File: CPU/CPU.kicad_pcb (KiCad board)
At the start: 2 copper layers, 157.1 x 85.3 mm, 100 parts, among them J101 Conn_02x10_Odd_Even, J102 Conn_02x14_Odd_Even_MountingP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, J301 Conn_02x03_Odd_Even, J302 1X4SMD-FPC, J303 Conn_02x03_Odd_Even, Q101 IRLML0040TR, Q102 IRLML0040TR, Q201 DMC4050, Q301 IRLML0040TR, Q302 IRLML0040TR, SW101 SW_SPDT, SW301 TACTILE_SWITCHPTS540-SMD, SW302 TACTILE_SWITCHPTS540-SMD, SW303 TACTILE_SWITCHPTS540-SMD, SW304 TACTILE_SWITCHPTS540-SMD, SW305 TACTILE_SWITCHPTS540-SMD, SW306 TACTILE_SWITCHPTS540-SMD, SW307 TACTILE_SWITCHPTS540-SMD, SW308 TACTILE_SWITCHPTS540-SMD, SW309 TACTILE_SWITCHPTS540-SMD, SW310 TACTILE_SWITCHPTS540-SMD, SW311 TACTILE_SWITCHPTS540-SMD, SW312 TACTILE_SWITCHPTS540-SMD, SW313 TACTILE_SWITCHPTS540-SMD, U201 OPT3001, U202 ATtiny1614-SS, U301 ATmega328PB-AU, Y301 Resonator_Small

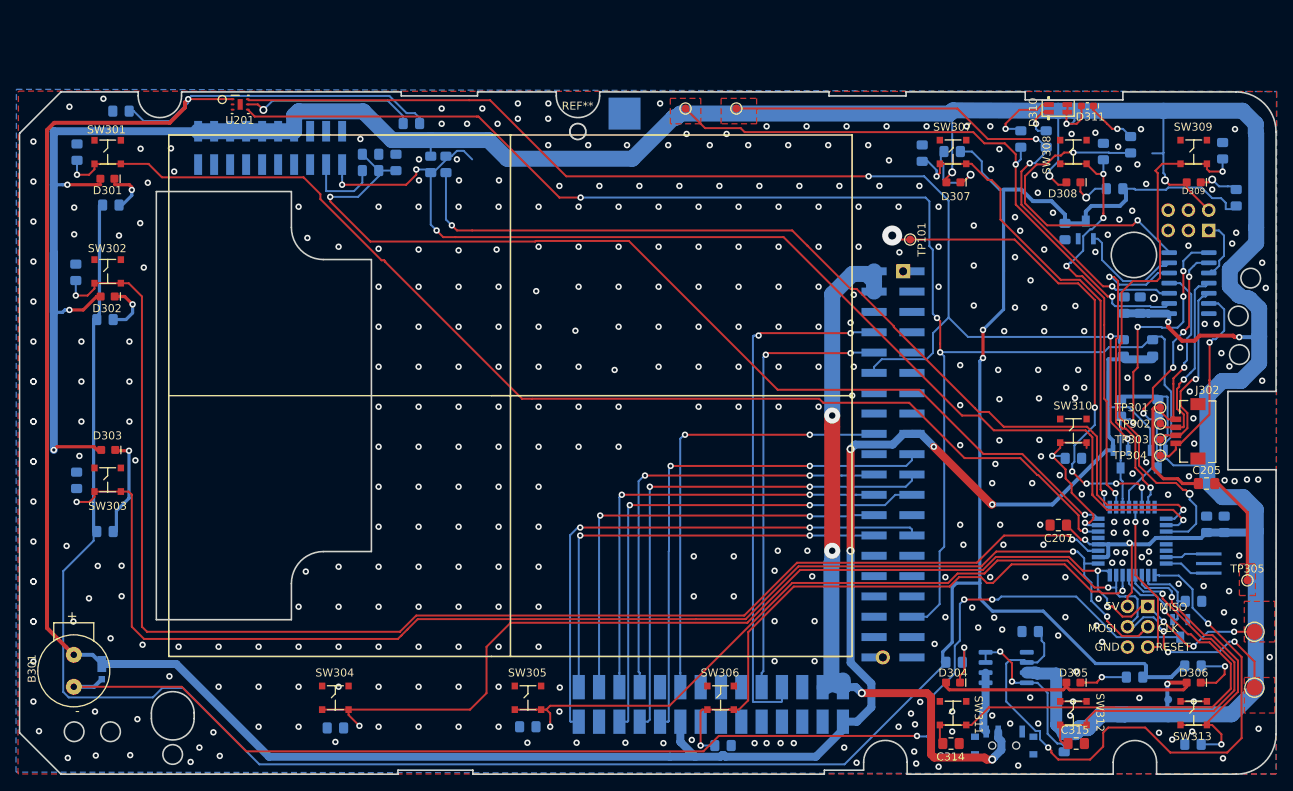
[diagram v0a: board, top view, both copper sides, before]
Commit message: Renaming components.
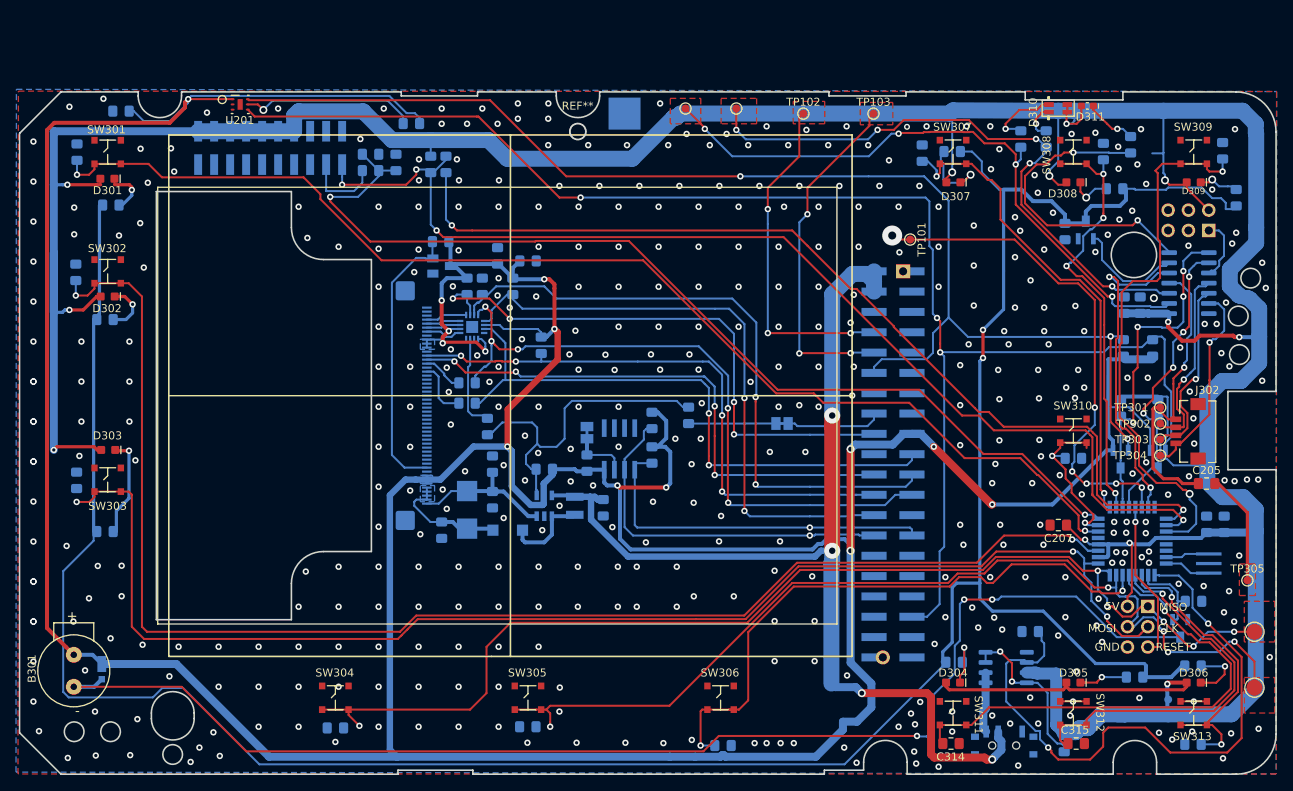
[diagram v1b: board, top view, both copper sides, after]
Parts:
- removed J102: Conn_02x14_Odd_Even_MountingPin, CPU:2X14_SMT_MALE-2
- added C1: 10uF, Capacitor_SMD:C_0805_2012Metric_Pad1.15x1.40mm_HandSolder, B.Cu at (94.0, 66.7)
- added C16: 10uF, Capacitor_SMD:C_0805_2012Metric_Pad1.15x1.40mm_HandSolder, B.Cu at (103.4, 97.5)
- added C18: 0.1uF, Capacitor_SMD:C_0805_2012Metric_Pad1.15x1.40mm_HandSolder, B.Cu at (89.5, 96.5)
- added C20: 1uF, Capacitor_SMD:C_0805_2012Metric_Pad1.15x1.40mm_HandSolder, B.Cu at (83.2, 100.3)
- added C4: 0.1uF, Capacitor_SMD:C_0805_2012Metric_Pad1.15x1.40mm_HandSolder, B.Cu at (90.2, 66.0)
- added D1: MM3Z24VT1G, PiTFT:SMADIODE, B.Cu at (86.4, 97.8)
- added D2: MBR0540, PiTFT:SOD-123, B.Cu at (91.4, 100.3)
- added IC5: AXP803, PiTFT:SOT23, B.Cu at (83.2, 67.3)
- added L1: 10uH 1007, PiTFT:INDUCTOR_1007, B.Cu at (99.8, 97.3)
- added R1: 12Ω, Resistor_SMD:R_0805_2012Metric_Pad1.15x1.40mm_HandSolder, B.Cu at (89.5, 92.1)
- added R10: 1K, Resistor_SMD:R_0805_2012Metric_Pad1.15x1.40mm_HandSolder, B.Cu at (114.0, 86.0)
- added R11: 10K, Resistor_SMD:R_0805_2012Metric_Pad1.15x1.40mm_HandSolder, B.Cu at (88.3, 69.8)
- added R12: 3.9K, Resistor_SMD:R_0805_2012Metric_Pad1.15x1.40mm_HandSolder, B.Cu at (109.5, 90.9)
- added R13: 3.9K, Resistor_SMD:R_0805_2012Metric_Pad1.15x1.40mm_HandSolder, B.Cu at (109.5, 86.6)
- added R14: 3.9K, Resistor_SMD:R_0805_2012Metric_Pad1.15x1.40mm_HandSolder, B.Cu at (101.3, 91.9)
- added R2: 10K, Resistor_SMD:R_0805_2012Metric_Pad1.15x1.40mm_HandSolder, B.Cu at (96.0, 92.7)
- added R3: 12, Resistor_SMD:R_0805_2012Metric_Pad1.15x1.40mm_HandSolder, B.Cu at (86.4, 84.5)
- added R4: 12, Resistor_SMD:R_0805_2012Metric_Pad1.15x1.40mm_HandSolder, B.Cu at (86.4, 81.9)
- added R5: 10K, Resistor_SMD:R_0805_2012Metric_Pad1.15x1.40mm_HandSolder, B.Cu at (95.6, 77.2)
- added R6: 10K, Resistor_SMD:R_0805_2012Metric_Pad1.15x1.40mm_HandSolder, B.Cu at (83.1, 64.3)
- added R7: 10K, Resistor_SMD:R_0805_2012Metric_Pad1.15x1.40mm_HandSolder, B.Cu at (92.1, 69.8)
- added R8: DNP, Resistor_SMD:R_0805_2012Metric_Pad1.15x1.40mm_HandSolder, B.Cu at (86.4, 69.8)
- added R9: 1K, Resistor_SMD:R_0805_2012Metric_Pad1.15x1.40mm_HandSolder, B.Cu at (88.9, 87.4)
- added SJ1: WP, PiTFT:SOLDERJUMPER_CLOSEDWIRE, B.Cu at (101.3, 88.1)
- added SJ2: SOLDERJUMPERCLOSED, PiTFT:SOLDERJUMPER_CLOSEDWIRE, B.Cu at (125.7, 87.0)
- added TP102: PiTX, TestPoint:TestPoint_Pad_D1.0mm, F.Cu at (128.4, 48.3)
- added TP103: PiRX, TestPoint:TestPoint_Pad_D1.0mm, F.Cu at (137.2, 48.3)
- added U1: CAT24C32, PiTFT:SOIC8_150MIL, B.Cu at (105.4, 90.2)
- added U2: STMPE610, PiTFT:QFN16_3MM, B.Cu at (87.0, 74.9)
- added U3: FAN5333BSX, PiTFT:SOT23-5@1, B.Cu at (96.0, 97.3)
- added X1: DISP_LCD_3.5IN_320X480_50PIN, PiTFT:TFT_3.5IN_320X480_50PIN, F.Cu at (85.1, 84.8)
- TP201: value TestPoint -> GND
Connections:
- Pi101 pad 10: /UARTB -> /PiRX
- Pi101 pad 16: Net-(Pi101-Pad16) -> /LCD_BACK_LIGHT
- Pi101 pad 8: /UARTA -> /PiTX
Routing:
- net +3V3: track 346.7 -> 556.3 mm, vias 5 -> 14
- net /UARTA: track 66.4 -> 0.00 mm, vias 2 -> 0
- net /UARTB: track 55.4 -> 0.00 mm, vias 2 -> 0
- net /PiRX: track 0.00 -> 43.2 mm, vias 0 -> 3
- net /PiTX: track 0.00 -> 42.6 mm, vias 0 -> 3
- net /Display/LCD_LITE: track 0.00 -> 40.9 mm
- net /Pi5V: track 92.0 -> 132.2 mm
- net /Display/TFT_RST: track 0.00 -> 35.2 mm
- net /EEDATA: track 68.3 -> 45.5 mm, vias 2 -> 1
- net /RT_CS: track 55.8 -> 76.3 mm
- net /SCLK: track 64.0 -> 83.6 mm, vias 2 -> 5
- net /Display/LEDK: track 0.00 -> 18.1 mm
- net /TFT_CS: track 55.7 -> 72.7 mm, vias 2 -> 4
- net /MISO: track 64.3 -> 80.7 mm
- net /RT_INIT: track 55.5 -> 71.8 mm, vias 2 -> 4
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- added copper zone on B.Cu, net +24V
- added copper zone on B.Cu, net +3V3
- added copper zone on F.Cu, net /PiRX
- added copper zone on F.Cu, net /PiTX
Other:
- board text added: "CR101 CPU Board V3 mquezada 20200519"
- board text removed: "CR101 CPU Board V2 mquezada 20200423"

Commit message: Add display circuitry.
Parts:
- D201: value Schottky -> Zener
- IC5: value AXP803 -> MAX803
- R3, R4: value 12 -> 12Ω
- U2: value STMPE610 -> STMPE811
- moved TP201 0.51 mm to (106.0, 48.8)
- moved C16 0.25 mm to (103.6, 97.5)
- turned R1 to 90 degrees
- turned R10 to 90 degrees
- turned R2 to 180 degrees
- turned R5 to 270 degrees
- turned R9 to 270 degrees
- renumbered C304 to C201, C305 to C202, C306 to C203, C307 to C204, C308 to C205, C309 to C206, C310 to C207, C311 to C208, C312 to C209, C313 to C210, C314 to C211, C315 to C212, C316 to C213, C206 to C214, C207 to C215, C301 to C216, C303 to C217, C201 to C301, C203 to C302, C202 to C303, C204 to C304, C205 to C305, J301 to J201, Q302 to Q202, R201 to R313, SW301 to SW201, SW302 to SW202, SW303 to SW203, SW304 to SW204, SW305 to SW205, SW306 to SW206, SW307 to SW207, SW308 to SW208, SW309 to SW209, SW310 to SW210, SW311 to SW211, SW312 to SW212, SW313 to SW213, U301 to U201, U201 to U301, U202 to U302, Y301 to Y201
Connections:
- R1 pad 1: GND -> /Display/LEDK
- R1 pad 2: /Display/LEDK -> GND
- R10 pad 1: /Display/LCD_LITE -> Net-(R10-Pad1)
- R10 pad 2: Net-(R10-Pad2) -> /Display/LCD_LITE
- R2 pad 1: /Display/LCD_LITE -> +3V3
- R2 pad 2: +3V3 -> /Display/LCD_LITE
- R5 pad 1: /TFT_CS -> +3V3
- R5 pad 2: +3V3 -> /TFT_CS
- R9 pad 1: /Display/LCD_LITE -> Net-(R9-Pad1)
- R9 pad 2: Net-(R9-Pad2) -> /Display/LCD_LITE
- SJ2 pad 2: Net-(R10-Pad2) -> Net-(R10-Pad1)
- U2 pad 11: Net-(R9-Pad2) -> Net-(R9-Pad1)
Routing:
- net Net-(R9-Pad2): track 11.8 -> 0.00 mm
- net Net-(R9-Pad1): track 0.00 -> 11.8 mm
- net Net-(R10-Pad2): track 10.9 -> 0.00 mm
- net Net-(R10-Pad1): track 0.00 -> 10.9 mm
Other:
- board text added: "LCD interface circuit by Adafruit. Referenced from PiTFT 3.5""

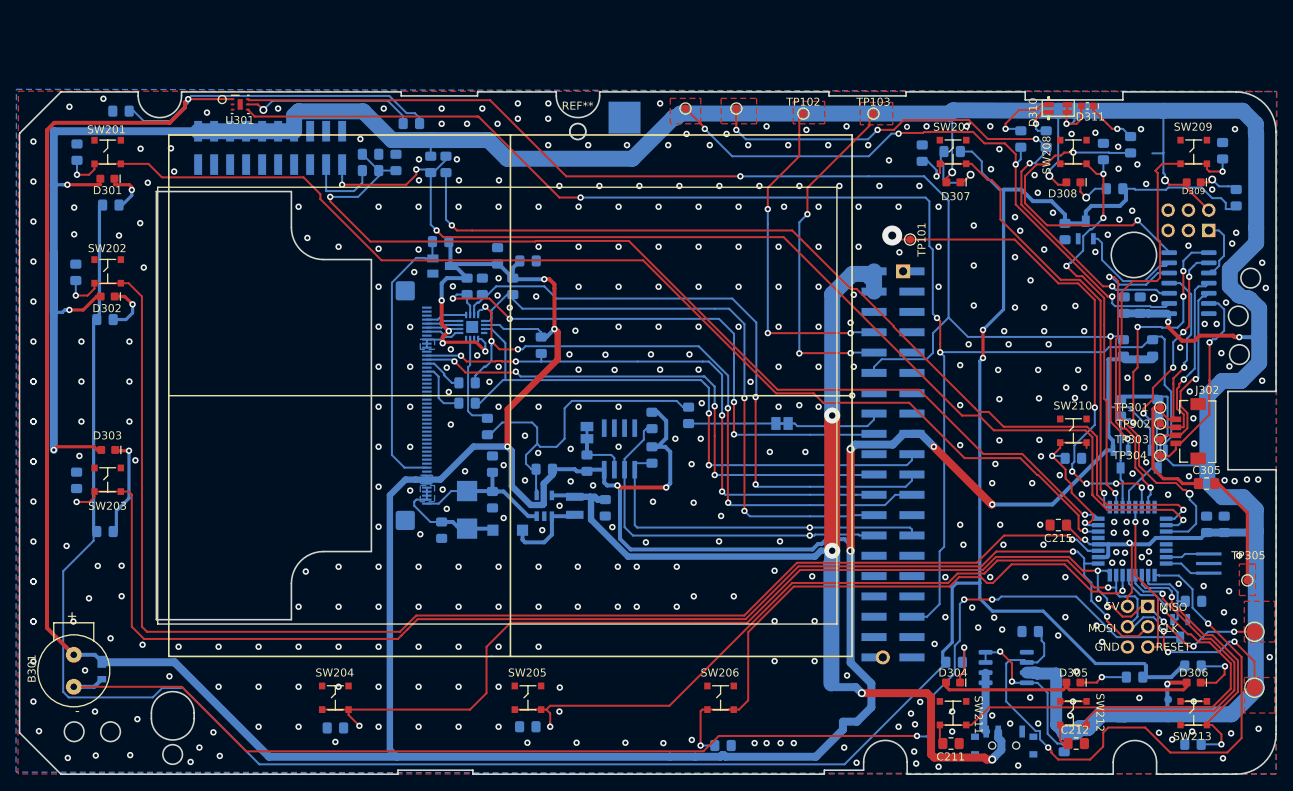
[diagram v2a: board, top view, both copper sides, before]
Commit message: Move to separate branch to track CPU development separately.
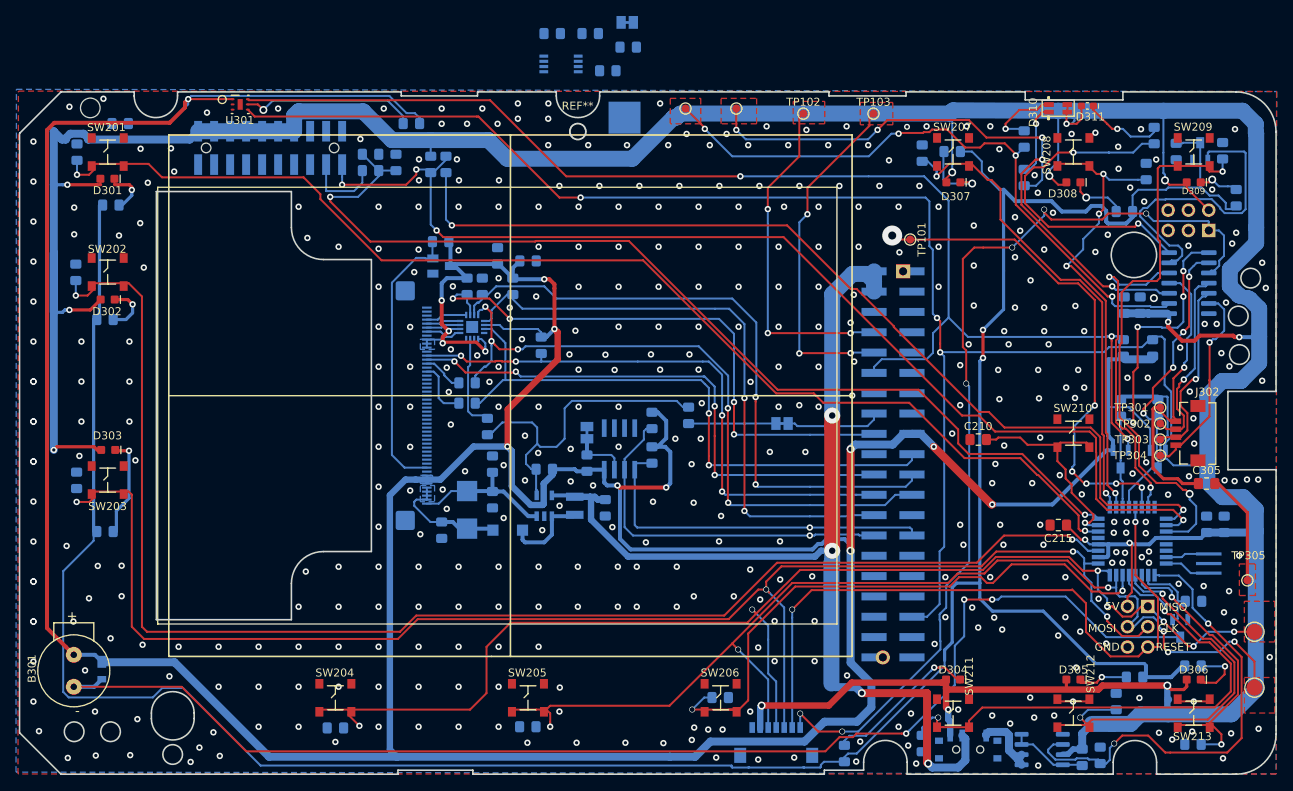
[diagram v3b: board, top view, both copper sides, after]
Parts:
- added C101: 10uF, Capacitor_SMD:C_0805_2012Metric_Pad1.15x1.40mm_HandSolder, B.Cu at (97.0, 38.2)
- added C102: 0.1uF, Capacitor_SMD:C_0805_2012Metric_Pad1.15x1.40mm_HandSolder, B.Cu at (104.0, 42.9)
- added C103: 10uF, Capacitor_SMD:C_0805_2012Metric_Pad1.15x1.40mm_HandSolder, B.Cu at (101.8, 38.2)
- added J102: Conn_01x07_Female, MarcoK:SM07B-SHLS-TF, B.Cu at (125.0, 126.5)
- added R105: 100K, Resistor_SMD:R_0805_2012Metric_Pad1.15x1.40mm_HandSolder, B.Cu at (106.5, 40.0)
- added SJ101: SOLDERJUMPERCLOSED, PiTFT:SOLDERJUMPER_CLOSEDWIRE, B.Cu at (106.4, 36.9)
- added U101: LP2989-3.3_SOIC8_VSSOP8, Package_SO:TSSOP-8_3x3mm_P0.65mm, B.Cu at (98.1, 42.0)
- C210: moved to F.Cu
- C211, C212: moved to B.Cu
- C215, C301: value 100nF -> 0.1uF
- R101, R102, R103, R104: value 10K -> 2.2K
- SJ1: value WP -> SOLDERJUMPERCLOSED
- moved R304 17.8 mm to (133.5, 128.2), turned to 90 degrees
- moved R209 17.8 mm to (165.5, 128.5), turned to 270 degrees
- moved Q301 17.3 mm to (178.0, 53.0)
- moved C304 17.1 mm to (175.0, 53.0)
- moved C210 12.1 mm to (150.2, 89.0), turned to 0 degrees
- moved Q201 11.2 mm to (158.2, 127.8)
- moved C212 7.25 mm to (167.5, 121.8), turned to 270 degrees
- moved C206 6.01 mm to (118.0, 121.2)
- moved C208 5.91 mm to (171.2, 55.5)
- moved R311 5.54 mm to (156.0, 56.2)
- moved SW101 4.53 mm to (149.0, 127.8)
- moved C211 3.60 mm to (143.2, 127.0), turned to 90 degrees
- moved R312 3.17 mm to (172.2, 51.0)
- moved R308 3.10 mm to (168.5, 60.5)
- moved R208 2.84 mm to (163.2, 128.7)
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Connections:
- net /I2C Devices/85RES renamed Net-(U201-Pad32)
- net /I2C Devices/UPDI renamed /PUPDI
- net /Micro Controller Devices/RST renamed /PRST
- net /Micro Controller Devices/SW- renamed /PSCK
- net /Micro Controller Devices/SWA renamed /PMISO
- net /Micro Controller Devices/SWB renamed /PMOSI
- Pi101 pad 13: Net-(Pi101-Pad13) -> /LCD_PWR
- SW101 pad 1: Net-(SW101-Pad1) -> +5VP
- SW101 pad 3: +5VP -> 5V
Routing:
- net /PUPDI: track 8.72 -> 120.4 mm, vias 0 -> 6
- net /PRST: track 19.9 -> 86.4 mm, vias 1 -> 2
- net /I2C Devices/LED_PWM: track 14.5 -> 38.6 mm
- net 5V: track 511.1 -> 532.7 mm, vias 12 -> 14
- net /Micro Controller Devices/PI_PWR_SW: track 78.0 -> 58.3 mm
- net /PSCK: track 167.0 -> 186.6 mm, vias 3 -> 4
- net /PMISO: track 140.6 -> 157.2 mm, vias 6 -> 7
- net Net-(D304-PadC): track 6.50 -> 19.6 mm
- net /PMOSI: track 120.5 -> 133.2 mm, vias 5 -> 6
- net Net-(Q201-Pad4): track 21.0 -> 9.94 mm, vias 2 -> 0
- net Net-(C304-Pad1): track 324.3 -> 334.8 mm
- net /Micro Controller Devices/SWE: track 20.8 -> 28.2 mm, vias 2 -> 1
- net /I2C Devices/GREEN: track 75.9 -> 81.1 mm
- net Net-(D310-Pad3): track 4.63 -> 9.34 mm
- net Net-(D311-PadC): track 6.53 -> 10.3 mm
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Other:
- outline, holes or cut-outs redrawn
- board text added: "SCL"
- board text added: "SDA"
- board text added: "U R C I O 5 G"

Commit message: Replacing the TFT. Before removing EEPROM and voltage monitor.
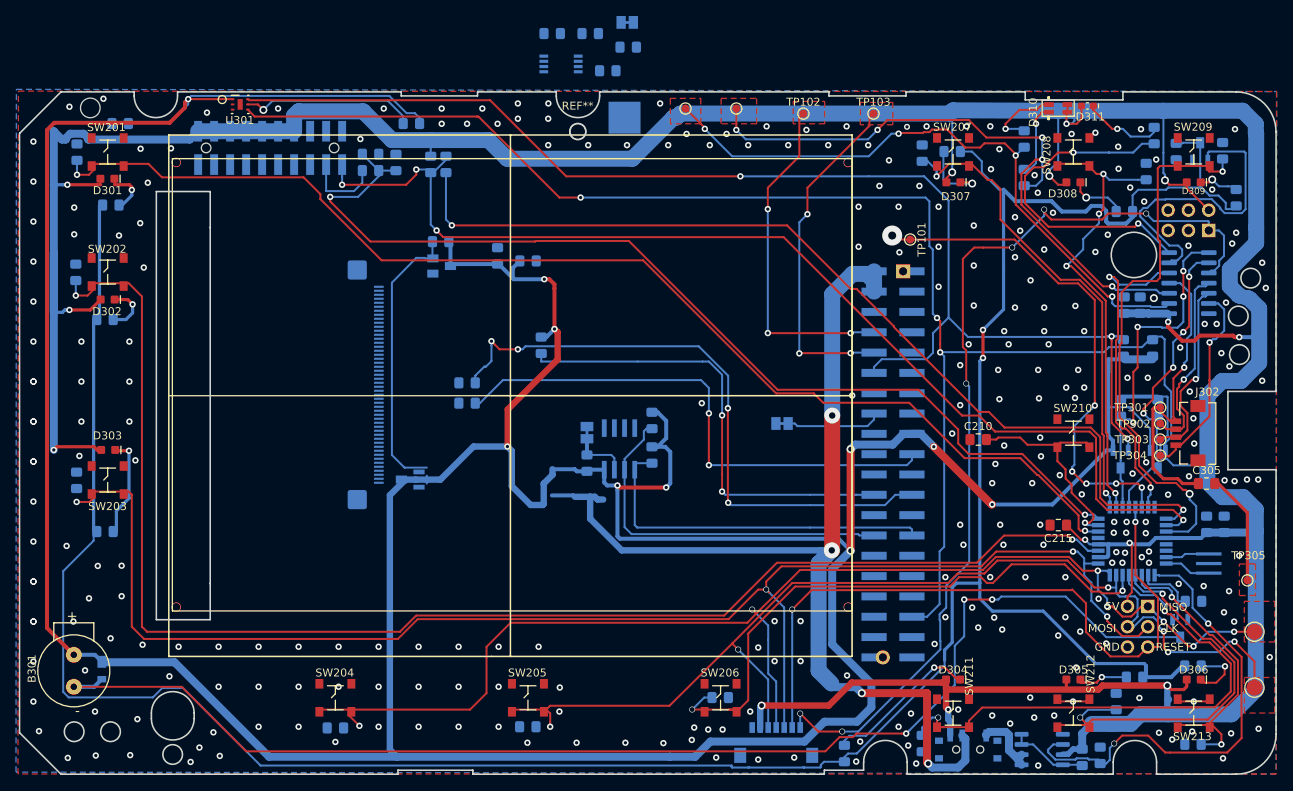
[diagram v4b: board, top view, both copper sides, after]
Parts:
- removed C16: 10uF, Capacitor_SMD:C_0805_2012Metric_Pad1.15x1.40mm_HandSolder
- removed C18: 0.1uF, Capacitor_SMD:C_0805_2012Metric_Pad1.15x1.40mm_HandSolder
- removed C20: 1uF, Capacitor_SMD:C_0805_2012Metric_Pad1.15x1.40mm_HandSolder
- removed D1: MM3Z24VT1G, PiTFT:SMADIODE
- removed D2: MBR0540, PiTFT:SOD-123
- removed L1: 10uH 1007, PiTFT:INDUCTOR_1007
- removed R1: 12Ω, Resistor_SMD:R_0805_2012Metric_Pad1.15x1.40mm_HandSolder
- removed R10, R9: 1K, Resistor_SMD:R_0805_2012Metric_Pad1.15x1.40mm_HandSolder
- removed R11, R2, R7: 10K, Resistor_SMD:R_0805_2012Metric_Pad1.15x1.40mm_HandSolder
- removed R8: DNP, Resistor_SMD:R_0805_2012Metric_Pad1.15x1.40mm_HandSolder
- removed U2: STMPE811, PiTFT:QFN16_3MM
- removed U3: FAN5333BSX, PiTFT:SOT23-5@1
- added Q401: IRLML0040TR, CPU:SOT23, B.Cu at (79.2, 94.0)
- X1: footprint PiTFT:TFT_3.5IN_320X480_50PIN -> CPU:TFT_3.5IN_320X480_50PIN_BUY_DISPLAY_ER-TFT035-6
- moved X1 7.39 mm to (92.0, 82.2)
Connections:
- X1 pad 1: /Display/LEDK -> +3V3
- X1 pad 2: +24V -> Net-(Q401-Pad3)
- X1 pad 3: +24V -> Net-(Q401-Pad3)
- X1 pad 4: +24V -> Net-(X1-Pad4)
- X1 pad 5: +24V -> Net-(X1-Pad5)
- X1 pad 6: +3V3 -> Net-(X1-Pad6)
- X1 pad 9: (no net) -> +3V3
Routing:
- net /MISO: track 80.7 -> 0.00 mm, vias 2 -> 0
- net /RT_CS: track 76.3 -> 0.00 mm, vias 2 -> 0
- net /RT_INIT: track 71.8 -> 0.00 mm, vias 4 -> 0
- net /TFT_DC: track 68.5 -> 0.00 mm, vias 4 -> 0
- net /Display/LCD_LITE: track 40.9 -> 0.00 mm
- net +3V3: track 554.7 -> 519.7 mm, vias 14 -> 10
- net /Display/LEDK: track 18.1 -> 0.00 mm
- net +24V: track 15.0 -> 0.00 mm
- net /TFT_CS: track 72.7 -> 58.1 mm, vias 4 -> 2
- net Net-(R9-Pad1): track 11.8 -> 0.00 mm
- net Net-(D2-PadA): track 11.2 -> 0.00 mm
- net Net-(R10-Pad1): track 10.9 -> 0.00 mm
- net /MOSI: track 74.9 -> 66.8 mm
- net Net-(R3-Pad2): track 7.21 -> 0.00 mm
- net /SCLK: track 83.6 -> 77.4 mm, vias 5 -> 4
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- removed copper zone on B.Cu, net +24V
- removed copper zone on B.Cu, net +3V3
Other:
- outline, holes or cut-outs redrawn
